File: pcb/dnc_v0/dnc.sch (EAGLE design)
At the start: 1 part

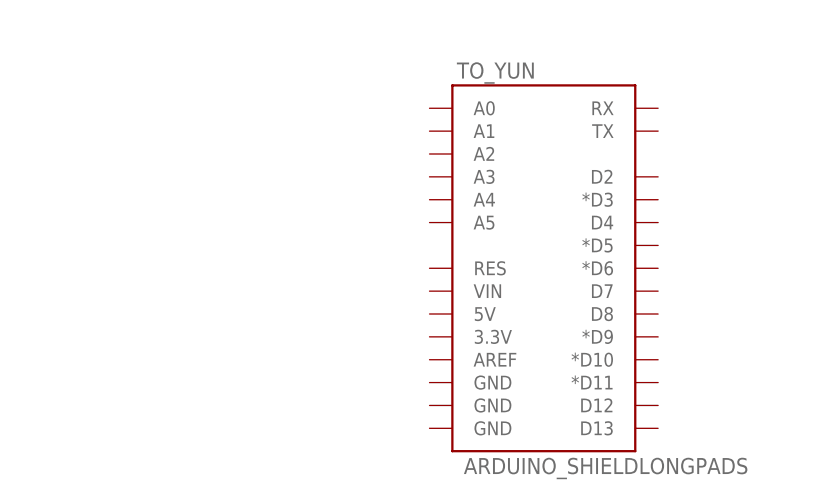
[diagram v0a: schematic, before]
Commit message: draw yunshield eagle-objet in a eaglelib pcb add sunshield eagle file in docref
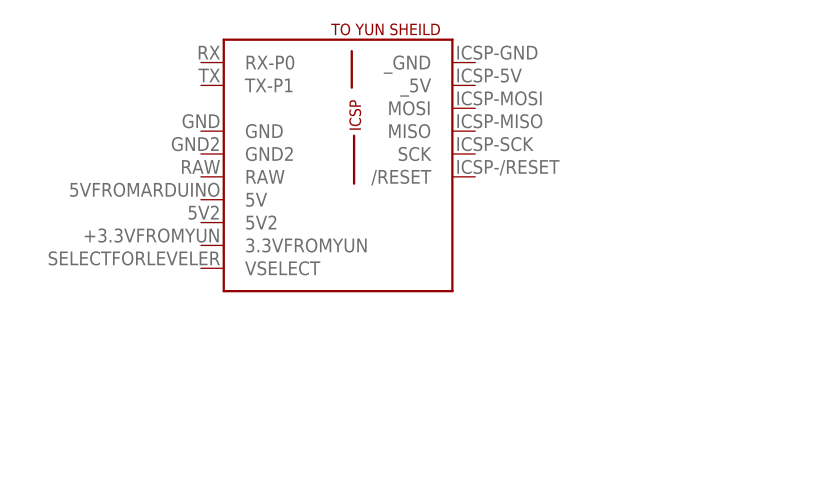
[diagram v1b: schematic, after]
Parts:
- removed TO_YUN: ARDUINO_SHIELDLONGPADS, SparkFun-Boards:ARDUINO_SHIELDLONGPADS
- added U$1: YUNBOARD_CONNECT, pierre_vv:YUNBOARD_CONNECT
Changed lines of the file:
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@@
 <layer number="54" name="bGND_GNDA" color="1" fill="9" visible="no" active="no"/>
 <layer number="56" name="wert" color="7" fill="1" visible="no" active="no"/>
+<layer number="57" name="tCAD" color="7" fill="1" visible="no" active="no"/>
 <layer number="90" name="Modules" color="5" fill="1" visible="yes" active="yes"/>
 <layer number="91" name="Nets" color="2" fill="1" visible="yes" active="yes"/>
@@
 <layer number="106" name="bPlate" color="7" fill="1" visible="yes" active="yes"/>
 <layer number="107" name="Crop" color="7" fill="1" visible="yes" active="yes"/>
+<layer number="108" name="fp8" color="7" fill="1" visible="no" active="yes"/>
+<layer number="109" name="fp9" color="7" fill="1" visible="no" active="yes"/>
+<layer number="110" name="fp0" color="7" fill="1" visible="no" active="yes"/>
+<layer number="111" name="111" color="7" fill="1" visible="no" active="yes"/>
+<layer number="112" name="tSilk" color="7" fill="1" visible="no" active="yes"/>
 <layer number="116" name="Patch_BOT" color="9" fill="4" visible="yes" active="yes"/>
+<layer number="118" name="Rect_Pads" color="7" fill="1" visible="no" active="yes"/>
 <layer number="121" name="_tsilk" color="7" fill="1" visible="yes" active="yes"/>
 <layer number="122" name="_bsilk" color="7" fill="1" visible="yes" active="yes"/>
+<layer number="123" name="tTestmark" color="7" fill="1" visible="no" active="yes"/>
+<layer number="124" name="bTestmark" color="7" fill="1" visible="no" active="yes"/>
 <layer number="125" name="_tNames" color="7" fill="1" visible="yes" active="yes"/>
+<layer number="126" name="_bNames" color="7" fill="1" visible="no" active="yes"/>
+<layer number="127" name="_tValues" color="7" fill="1" visible="no" active="yes"/>
+<layer number="128" name="_bValues" color="7" fill="1" visible="no" active="yes"/>
+<layer number="131" name="tAdjust" color="7" fill="1" visible="no" active="yes"/>
+<layer number="132" name="bAdjust" color="7" fill="1" visible="no" active="yes"/>
 <layer number="144" name="Drill_legend" color="7" fill="1" visible="yes" active="yes"/>
+<layer number="150" name="Notes" color="7" fill="1" visible="no" active="yes"/>
 <layer number="151" name="HeatSink" color="7" fill="1" visible="yes" active="yes"/>
+<layer number="152" name="_bDocu" color="7" fill="1" visible="no" active="yes"/>
+<layer number="153" name="FabDoc1" color="7" fill="1" visible="no" active="yes"/>
+<layer number="154" name="FabDoc2" color="7" fill="1" visible="no" active="yes"/>
+<layer number="155" name="FabDoc3" color="7" fill="1" visible="no" active="yes"/>
+<layer number="199" name="Contour" color="7" fill="1" visible="no" active="yes"/>
 <layer number="200" name="200bmp" color="1" fill="10" visible="yes" active="yes"/>
 <layer number="201" name="201bmp" color="2" fill="10" visible="yes" active="yes"/>
@@
 <layer number="223" name="223bmp" color="24" fill="1" visible="no" active="no"/>
 <layer number="224" name="224bmp" color="25" fill="1" visible="no" active="no"/>
+<layer number="248" name="Housing" color="7" fill="1" visible="no" active="yes"/>
+<layer number="249" name="Edge" color="7" fill="1" visible="no" active="yes"/>
 <layer number="250" name="Descript" color="3" fill="1" visible="no" active="no"/>
 <layer number="251" name="SMDround" color="12" fill="11" visible="no" active="no"/>
@@
 </classes>
 <parts>
-<part name="TO_YUN" library="SparkFun-Boards" deviceset="ARDUINO_SHIELD" device="LONGPADS"/>
+<part name="U$1" library="pierre_vv" deviceset="YUNBOARD_CONNECT" device=""/>
 </parts>
 <sheets>
@@
 </plain>
 <instances>
-<instance part="TO_YUN" gate="G$1" x="10.16" y="63.5"/>
+<instance part="U$1" gate="G$1" x="-12.7" y="73.66"/>
 </instances>
 <busses>

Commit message: Avancée sur eagle
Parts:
- added IC1: 74HC595D, 74xx-eu:74HC595D
- added JP1: (no value), SparkFun-Connectors:M02-JST-2-PTH-NO_SILK
- added RCODE: (no value), SparkFun-Passives:RESISTOR2512
- added U1: ATMEGA168, SparkFun:ATMEGA168
- added X1, X2, X3, X4, X5, X6, X7, X8: 332-12, con-garry:332-12
- added Y1: 16MHZ, SparkFun-FreqCtrl:RESONATOR16MHZ
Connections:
- new net /REGCLEAR: IC1A.SCL
- new net /REGENABLE: IC1A.G
- new net /RESET: U$1./RESET, U1.PC6(/RESET)
- new net CODE: RCODE.1, U1.PC0(ADC0), X1-8.S, X2-8.S, X3-8.S, X4-8.S, X5-8.S, X6-8.S, X7-8.S, X8-8.S
- new net CS1: X1-7.S
- new net CS2: X2-7.S
- new net CS3: X3-7.S
- new net CS4: X4-7.S
- new net CS5: X5-7.S
- new net CS6: X6-7.S
- new net CS7: X7-7.S
- new net CS8: X8-7.S
- new net GND: RCODE.2, U$1.GND, U$1.GND2, U$1._GND, U1.AGND, U1.GND@1, U1.GND@2, X1-6.S, X2-6.S, X3-6.S, X4-6.S, X5-6.S, X6-6.S, X7-6.S, X8-6.S, Y1.2
- new net GND2: X1-10.S, X2-10.S, X3-10.S, X4-10.S, X5-10.S, X6-10.S, X7-10.S, X8-10.S
- new net GND3: X1-12.S, X2-12.S, X3-12.S, X4-12.S, X5-12.S, X6-12.S, X7-12.S, X8-12.S
- new net MISO: U$1.MISO, U1.PB4(MISO), X1-1.S, X2-1.S, X3-1.S, X4-1.S, X5-1.S, X6-1.S, X7-1.S, X8-1.S
- new net MOSI: U$1.MOSI, U1.PB3(MOSI/OC2), X1-4.S, X2-4.S, X3-4.S, X4-4.S, X5-4.S, X6-4.S, X7-4.S, X8-4.S
- new net N$1: U1.PB7(XTAL2/TOSC2), Y1.3
- new net N$2: U1.PB6(XTAL1/TOSC1), Y1.1
- new net N$6: U1.PB2(SS/OC1B)
- new net REGSHIFT: IC1A.RCK
- new net REGVAL: IC1A.SER
- new net RST1: IC1A.QA, X1-5.S
- new net RST2: IC1A.QB, X2-5.S
- new net RST3: IC1A.QC, X3-5.S
- new net RST4: IC1A.QD, X4-5.S
- new net RST5: IC1A.QE, X5-5.S
- new net RST6: IC1A.QF, X6-5.S
- new net RST7: IC1A.QG, X7-5.S
- new net RST8: IC1A.QH, X8-5.S
- new net RX: U$1.RX-P0, U1.PD0(RXD)
- new net SCK: IC1A.SCK, U$1.SCK, U1.PB5(SCK), X1-3.S, X2-3.S, X3-3.S, X4-3.S, X5-3.S, X6-3.S, X7-3.S, X8-3.S
- new net TX: U$1.TX-P1, U1.PD1(TXD)
- new net VCC: U$1._5V, U1.AREF, U1.AVCC, U1.VCC@1, U1.VCC@2, X1-2.S, X2-2.S, X3-2.S, X4-2.S, X5-2.S, X6-2.S, X7-2.S, X8-2.S
- new net VCC2: X1-9.S, X2-9.S, X3-9.S, X4-9.S, X5-9.S, X6-9.S, X7-9.S, X8-9.S
- new net VCC3: X1-11.S, X2-11.S, X3-11.S, X4-11.S, X5-11.S, X6-11.S, X7-11.S, X8-11.S

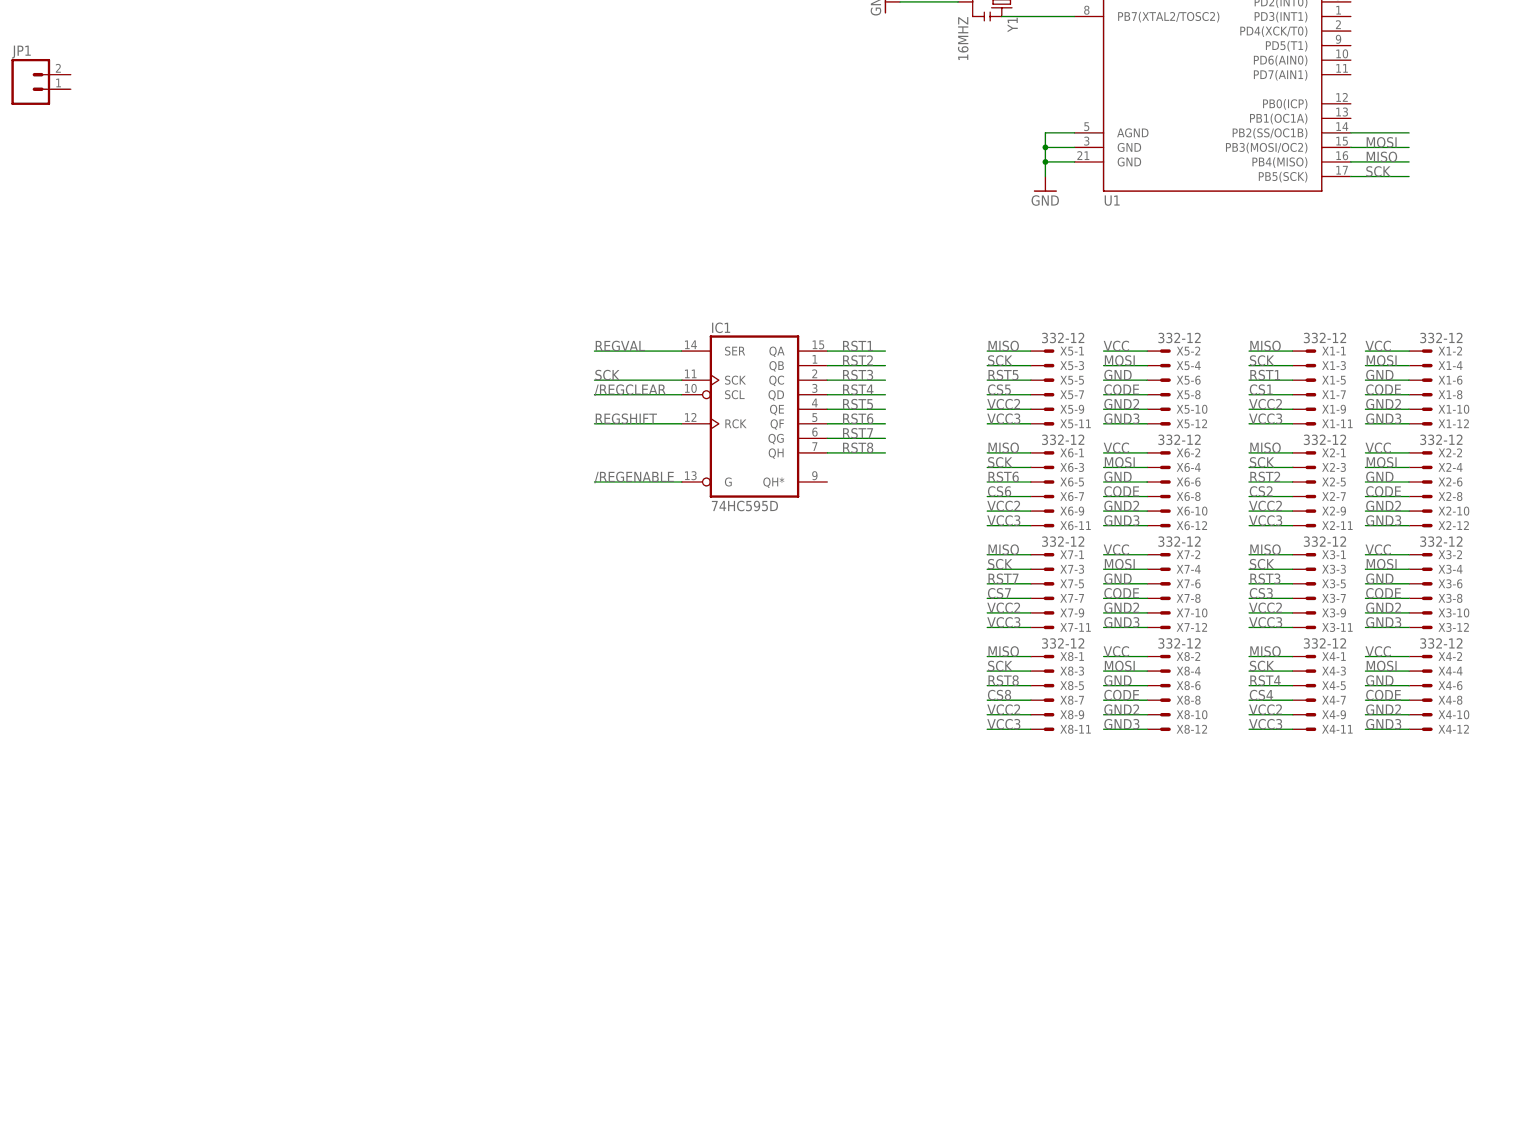
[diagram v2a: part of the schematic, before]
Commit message: Début de la modification pour RASPIA+
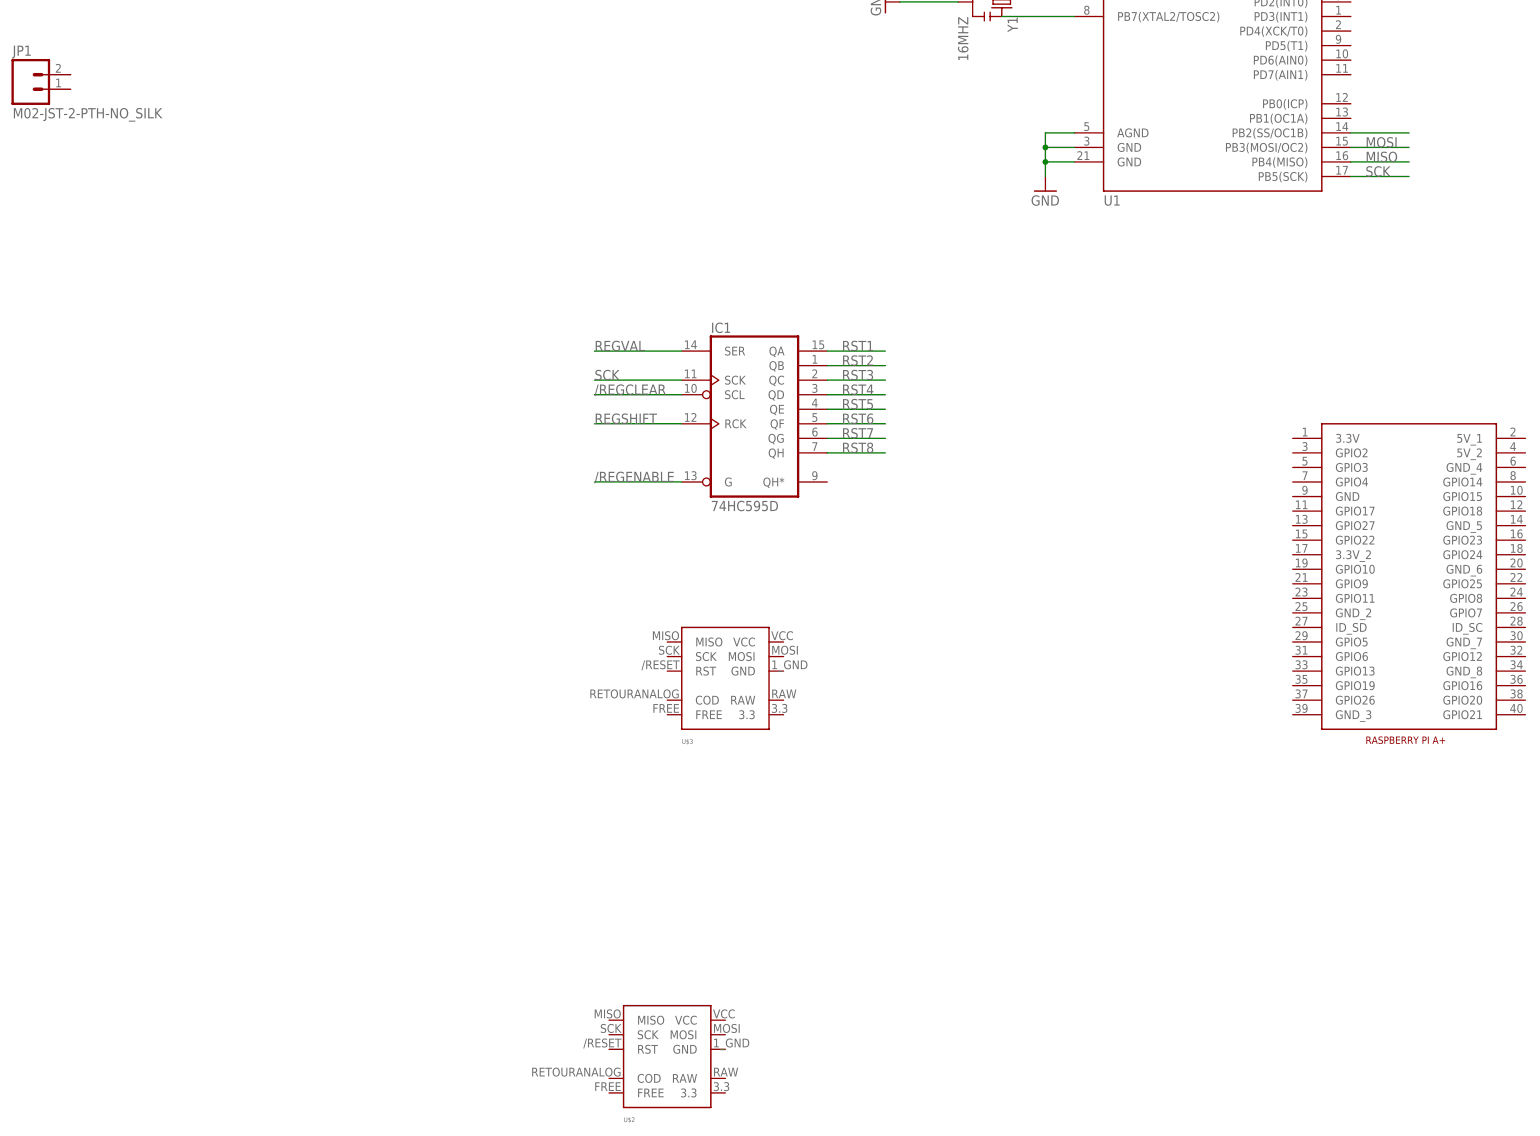
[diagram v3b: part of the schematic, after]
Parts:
- removed X1, X2, X3, X4, X5, X6, X7, X8: 332-12, con-garry:332-12
- added U$2, U$3: EXT-DNC, pierre_vv:EXT-DNC
- added U$4: RASPIA+, pierre_vv:RASPIA+
- JP1: value (none) -> M02-JST-2-PTH-NO_SILK
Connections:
- removed net CS1: X1-7.S
- removed net CS2: X2-7.S
- removed net CS3: X3-7.S
- removed net CS4: X4-7.S
- removed net CS5: X5-7.S
- removed net CS6: X6-7.S
- removed net CS7: X7-7.S
- removed net CS8: X8-7.S
- removed net GND2: X1-10.S, X2-10.S, X3-10.S, X4-10.S, X5-10.S, X6-10.S, X7-10.S, X8-10.S
- removed net GND3: X1-12.S, X2-12.S, X3-12.S, X4-12.S, X5-12.S, X6-12.S, X7-12.S, X8-12.S
- removed net VCC2: X1-9.S, X2-9.S, X3-9.S, X4-9.S, X5-9.S, X6-9.S, X7-9.S, X8-9.S
- removed net VCC3: X1-11.S, X2-11.S, X3-11.S, X4-11.S, X5-11.S, X6-11.S, X7-11.S, X8-11.S
- net CODE: no longer X1-8.S, X2-8.S, X3-8.S, X4-8.S, X5-8.S, X6-8.S, X7-8.S, X8-8.S
- net GND: no longer X1-6.S, X2-6.S, X3-6.S, X4-6.S, X5-6.S, X6-6.S, X7-6.S, X8-6.S
- net MISO: no longer X1-1.S, X2-1.S, X3-1.S, X4-1.S, X5-1.S, X6-1.S, X7-1.S, X8-1.S
- net MOSI: no longer X1-4.S, X2-4.S, X3-4.S, X4-4.S, X5-4.S, X6-4.S, X7-4.S, X8-4.S
- net RST1: no longer X1-5.S
- net RST2: no longer X2-5.S
- net RST3: no longer X3-5.S
- net RST4: no longer X4-5.S
- net RST5: no longer X5-5.S
- net RST6: no longer X6-5.S
- net RST7: no longer X7-5.S
- net RST8: no longer X8-5.S
- net SCK: no longer X1-3.S, X2-3.S, X3-3.S, X4-3.S, X5-3.S, X6-3.S, X7-3.S, X8-3.S
- net VCC: no longer X1-2.S, X2-2.S, X3-2.S, X4-2.S, X5-2.S, X6-2.S, X7-2.S, X8-2.S

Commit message: Progression sur le sch : 6x10pin + DC/DC + ANALOG_BAT
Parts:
- added IC2: 74HC595D, 74xx-eu:74HC595D
- added Q1: MOSFET-NCHANNEL_DUALFDMA1024NZ, SparkFun-DiscreteSemi:MOSFET-NCHANNEL_DUALFDMA1024NZ
- added R1, R2: (no value), SparkFun-Passives:RESISTOR1206
- added U$5: DC/DC_SEED, pierre_vv:DC/DC_SEED
- added U$6, U$7, U$8: EXT-DNC, pierre_vv:EXT-DNC
- U$1: value YUNBOARD_CONNECT -> EXT-DNC; device pierre_vv:YUNBOARD_CONNECT -> pierre_vv:EXT-DNC
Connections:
- removed net /REGCLEAR: IC1A.SCL
- removed net /REGENABLE: IC1A.G
- removed net REGSHIFT: IC1A.RCK
- removed net REGVAL: IC1A.SER
- new net /CS_EXT_1: U$3.RST
- new net /CS_EXT_2: U$1.RST
- new net /CS_EXT_3: U$2.RST
- new net /CS_EXT_4: U$6.RST
- new net /CS_EXT_5: U$7.RST
- new net /CS_EXT_6: U$8.RST
- new net 3.3: U$1.3.3, U$2.3.3, U$3.3.3, U$6.3.3, U$7.3.3, U$8.3.3
- new net 5V: U$4.5V_1, U$4.5V_2, U$5.OUT+
- new net ACTIVE_ANALOG_RAW: Q1A.G, U1.PD4(XCK/T0)
- new net ANALOG_RAW: Q1A.S, R2.2, U1.PC1(ADC1)
- new net N$10: U$8.FREE
- new net N$13: U$4.GPIO2
- new net N$14: U$4.GPIO3
- new net N$15: U$4.GPIO4
- new net N$16: U$4.GPIO17
- new net N$17: U$4.GPIO27
- new net N$18: U$4.GPIO22
- new net N$21: U$3.FREE
- new net N$23: U$4.ID_SD
- new net N$27: U$4.GPIO19
- new net N$28: U$4.GPIO26
- new net N$3: Q1A.D1, R1.1
- new net N$31: U$4.GPIO14
- new net N$32: U$4.GPIO15
- new net N$33: U$4.GPIO18
- new net N$34: U$4.GPIO23
- new net N$35: U$4.GPIO24
- new net N$36: U$4.GPIO25
- new net N$37: U$4.GPIO8
- new net N$38: U$4.GPIO7
- new net N$39: U$4.ID_SC
- new net N$4: U$1.FREE
- new net N$40: U$4.GPIO12
- new net N$41: U$4.GPIO16
- new net N$42: U$4.GPIO20
- new net N$43: U$4.GPIO21
- new net N$5: U$2.FREE
- new net N$7: IC1A.QH*, IC2A.SER
- new net N$8: U$6.FREE
- new net N$9: U$7.FREE
- new net RAW: JP1.1, R1.2, U$1.RAW, U$2.RAW, U$3.RAW, U$5.IN+, U$6.RAW, U$7.RAW, U$8.RAW
- new net REG_RCK: IC1A.RCK, IC2A.RCK, U$4.GPIO6
- new net REG_SCK: IC1A.SCK, IC2A.SCK, U$4.GPIO5
- new net REG_VAL: IC1A.SER, U$4.GPIO13
- new net RST10: IC2A.QB
- new net RST11: IC2A.QC
- new net RST12: IC2A.QD
- new net RST13: IC2A.QE
- new net RST14: IC2A.QF
- new net RST15: IC2A.QG
- new net RST16: IC2A.QH
- new net RST9: IC2A.QA
- net /RESET: no longer U$1./RESET
- net CODE: now also U$1.COD, U$2.COD, U$3.COD, U$6.COD, U$7.COD, U$8.COD
- net GND: now also JP1.2, R2.1, U$2.GND, U$3.GND, U$4.GND, U$4.GND_2, U$4.GND_3, U$4.GND_4, U$4.GND_5, U$4.GND_6, U$4.GND_7, U$4.GND_8, U$5.IN-, U$5.OUT-, U$6.GND, U$7.GND, U$8.GND; no longer U$1.GND2, U$1._GND
- net MISO: now also U$2.MISO, U$3.MISO, U$4.GPIO9, U$6.MISO, U$7.MISO, U$8.MISO
- net MOSI: now also U$2.MOSI, U$3.MOSI, U$4.GPIO10, U$6.MOSI, U$7.MOSI, U$8.MOSI
- net RX: no longer U$1.RX-P0
- net SCK: now also U$2.SCK, U$3.SCK, U$4.GPIO11, U$6.SCK, U$7.SCK, U$8.SCK; no longer IC1A.SCK
- net TX: no longer U$1.TX-P1
- net VCC: now also U$1.VCC, U$2.VCC, U$3.VCC, U$4.3.3V, U$4.3.3V_2, U$6.VCC, U$7.VCC, U$8.VCC; no longer U$1._5V
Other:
- moved on the sheet: U$2, U$3
